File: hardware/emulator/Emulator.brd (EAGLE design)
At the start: 69.6 x 71 mm, 41 parts, among them T2 2N5401, U2 LM6132BIN, U3 OPA2277PA, U4 L7908CV, U5 L7808ABV, U7 ZVP2106ASTZ, U8 DEV-16771_REDUCED_PINS, U9 MCP4822-E/P

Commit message: Add minor changes to the hardware
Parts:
- R_RANGE: value 51R -> 49R9
- moved C5 0.51 mm to (28.4, 23.1)
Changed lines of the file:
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@@
 <attribute name="VALUE" x="53.72099375" y="32.2326" size="1.27" layer="25" ratio="10" rot="R270"/>
 </element>
-<element name="R_RANGE" library="rcl" library_urn="urn:adsk.eagle:library:334" package="0207/10" package3d_urn="urn:adsk.eagle:package:23491/2" value="51R" x="48.93733125" y="30.988" smashed="yes" rot="R270">
+<element name="R_RANGE" library="rcl" library_urn="urn:adsk.eagle:library:334" package="0207/10" package3d_urn="urn:adsk.eagle:package:23491/2" value="49R9" x="48.93733125" y="30.988" smashed="yes" rot="R270">
 <attribute name="NAME" x="48.30233125" y="43.561" size="1.016" layer="25" ratio="10" rot="R270"/>
 <attribute name="POPULARITY" value="81" x="43.85733125" y="67.564" size="1.778" layer="27" rot="R270" display="off"/>
 <attribute name="SPICEPREFIX" value="R" x="43.85733125" y="67.564" size="1.778" layer="27" rot="R270" display="off"/>
-<attribute name="VALUE" x="48.30233125" y="32.2326" size="1.27" layer="25" ratio="10" rot="R270"/>
+<attribute name="VALUE" x="48.30233125" y="33.2486" size="1.27" layer="25" ratio="10" rot="R270"/>
 </element>
 <element name="R7" library="rcl" library_urn="urn:adsk.eagle:library:334" package="0207/10" package3d_urn="urn:adsk.eagle:package:23491/2" value="100R" x="51.6466625" y="30.988" smashed="yes" rot="R270">
@@
 <attribute name="POPULARITY" value="81" x="56.7266625" y="50.8" size="1.778" layer="27" rot="R270" display="off"/>
 <attribute name="SPICEPREFIX" value="R" x="56.7266625" y="50.8" size="1.778" layer="27" rot="R270" display="off"/>
-<attribute name="VALUE" x="51.0116625" y="33.2486" size="1.27" layer="25" ratio="10" rot="R270"/>
+<attribute name="VALUE" x="51.0116625" y="33.6296" size="1.27" layer="25" ratio="10" rot="R270"/>
 </element>
 <element name="U7" library="ZVP2106A" package="TO92-SGD" value="ZVP2106ASTZ" x="60.452" y="39.624" smashed="yes" rot="R90">
@@
 </element>
 <element name="C4" library="rcl" library_urn="urn:adsk.eagle:library:334" package="C025-024X044" package3d_urn="urn:adsk.eagle:package:23630/1" value="0.1u" x="42.418" y="31.242" smashed="yes" rot="R90">
-<attribute name="NAME" x="43.688" y="34.925" size="1.016" layer="25" ratio="10" rot="R180"/>
+<attribute name="NAME" x="43.18" y="34.798" size="1.016" layer="25" ratio="10" rot="R180"/>
 <attribute name="POPULARITY" value="56" x="42.418" y="31.242" size="1.778" layer="27" rot="R90" display="off"/>
 <attribute name="SPICEPREFIX" value="C" x="42.418" y="31.242" size="1.778" layer="27" rot="R90" display="off"/>
-<attribute name="VALUE" x="43.815" y="33.02" size="1.016" layer="27" ratio="10" rot="R270"/>
-</element>
-<element name="C5" library="rcl" library_urn="urn:adsk.eagle:library:334" package="C025-024X044" package3d_urn="urn:adsk.eagle:package:23630/1" value="0.1u" x="28.448" y="23.622" smashed="yes" rot="R90">
-<attribute name="NAME" x="29.083" y="21.209" size="1.016" layer="25" ratio="10" rot="R180"/>
-<attribute name="POPULARITY" value="56" x="28.448" y="23.622" size="1.778" layer="27" rot="R90" display="off"/>
-<attribute name="SPICEPREFIX" value="C" x="28.448" y="23.622" size="1.778" layer="27" rot="R90" display="off"/>
-<attribute name="VALUE" x="27.051" y="22.352" size="1.016" layer="25" ratio="10" rot="R90"/>
+<attribute name="VALUE" x="41.021" y="27.813" size="1.016" layer="25" ratio="10"/>
+</element>
+<element name="C5" library="rcl" library_urn="urn:adsk.eagle:library:334" package="C025-024X044" package3d_urn="urn:adsk.eagle:package:23630/1" value="0.1u" x="28.448" y="23.114" smashed="yes" rot="R90">
+<attribute name="NAME" x="29.083" y="20.701" size="1.016" layer="25" ratio="10" rot="R180"/>
+<attribute name="POPULARITY" value="56" x="28.448" y="23.114" size="1.778" layer="27" rot="R90" display="off"/>
+<attribute name="SPICEPREFIX" value="C" x="28.448" y="23.114" size="1.778" layer="27" rot="R90" display="off"/>
+<attribute name="VALUE" x="27.051" y="21.844" size="1.016" layer="25" ratio="10" rot="R90"/>
 </element>
 <element name="C6" library="rcl" library_urn="urn:adsk.eagle:library:334" package="C025-024X044" package3d_urn="urn:adsk.eagle:package:23630/1" value="0.1u" x="61.214" y="19.177" smashed="yes">
-<attribute name="NAME" x="58.801" y="17.907" size="1.016" layer="25" ratio="10" rot="R90"/>
+<attribute name="NAME" x="58.801" y="18.288" size="1.016" layer="25" ratio="10" rot="R90"/>
 <attribute name="POPULARITY" value="56" x="61.214" y="19.177" size="1.778" layer="27" display="off"/>
 <attribute name="SPICEPREFIX" value="C" x="61.214" y="19.177" size="1.778" layer="27" display="off"/>
-<attribute name="VALUE" x="59.944" y="16.51" size="1.016" layer="27" ratio="10"/>
+<attribute name="VALUE" x="59.944" y="16.51" size="1.016" layer="25" ratio="10"/>
 </element>
 <element name="R6" library="rcl" library_urn="urn:adsk.eagle:library:334" package="0207/10" package3d_urn="urn:adsk.eagle:package:23491/2" value="330R" x="51.816" y="61.468" smashed="yes" rot="R180">
-<attribute name="NAME" x="52.832" y="64.008" size="1.016" layer="25" ratio="10" rot="R180"/>
+<attribute name="NAME" x="52.324" y="64.008" size="1.016" layer="25" ratio="10" rot="R180"/>
 <attribute name="POPULARITY" value="81" x="51.816" y="54.356" size="1.778" layer="27" rot="R180" display="off"/>
 <attribute name="SPICEPREFIX" value="R" x="51.816" y="54.356" size="1.778" layer="27" rot="R180" display="off"/>
@@
 </element>
 <element name="R11" library="rcl" library_urn="urn:adsk.eagle:library:334" package="0207/10" package3d_urn="urn:adsk.eagle:package:23491/2" value="330R" x="51.816" y="57.912" smashed="yes" rot="R180">
-<attribute name="NAME" x="53.34" y="56.388" size="1.016" layer="25" ratio="10" rot="R180"/>
+<attribute name="NAME" x="52.832" y="56.388" size="1.016" layer="25" ratio="10" rot="R180"/>
 <attribute name="POPULARITY" value="81" x="51.816" y="50.8" size="1.778" layer="27" rot="R180" display="off"/>
 <attribute name="SPICEPREFIX" value="R" x="51.816" y="50.8" size="1.778" layer="27" rot="R180" display="off"/>
@@
 <wire x1="44.45" y1="15.748" x2="40.132" y2="15.748" width="1.27" layer="1"/>
 <wire x1="40.132" y1="15.748" x2="39.878" y2="16.002" width="1.27" layer="1"/>
-<wire x1="28.448" y1="24.892" x2="31.496" y2="24.892" width="1.27" layer="1"/>
+<wire x1="31.496" y1="24.892" x2="28.956" y2="24.892" width="1.27" layer="1"/>
+<wire x1="28.956" y1="24.892" x2="28.448" y2="24.384" width="1.27" layer="1"/>
 <wire x1="31.496" y1="24.892" x2="31.496" y2="22.987" width="1.27" layer="1"/>
 <wire x1="39.878" y1="16.002" x2="39.878" y2="13.114" width="1.27" layer="1"/>
@@
 <wire x1="27.051" y1="32.512" x2="31.496" y2="32.512" width="1.27" layer="1"/>
 <wire x1="27.051" y1="32.512" x2="25.908" y2="31.369" width="1.27" layer="1"/>
-<wire x1="25.908" y1="31.369" x2="25.908" y2="21.844" width="1.27" layer="1"/>
-<wire x1="25.908" y1="21.844" x2="28.067" y2="19.685" width="1.27" layer="1"/>
-<wire x1="28.067" y1="19.685" x2="29.591" y2="19.685" width="1.27" layer="1"/>
-<wire x1="29.591" y1="19.685" x2="38.608" y2="10.668" width="1.27" layer="1"/>
+<wire x1="25.908" y1="31.369" x2="25.908" y2="21.336" width="1.27" layer="1"/>
+<wire x1="25.908" y1="21.336" x2="28.321" y2="18.923" width="1.27" layer="1"/>
+<wire x1="28.321" y1="18.923" x2="30.353" y2="18.923" width="1.27" layer="1"/>
+<wire x1="30.353" y1="18.923" x2="38.608" y2="10.668" width="1.27" layer="1"/>
 <wire x1="38.608" y1="10.668" x2="41.369" y2="10.668" width="1.27" layer="1"/>
 <wire x1="41.369" y1="10.668" x2="42.418" y2="11.717" width="1.27" layer="1"/>

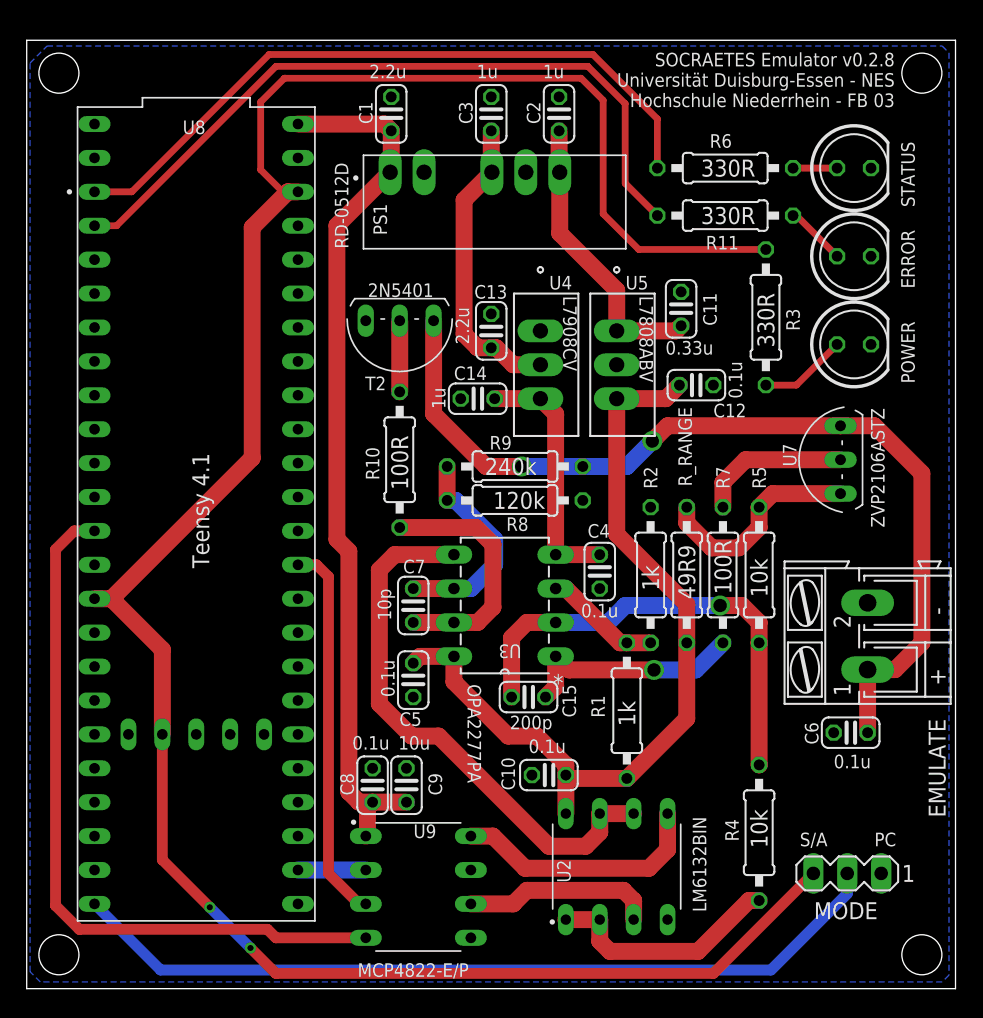
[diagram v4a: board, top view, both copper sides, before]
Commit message: Update part designators
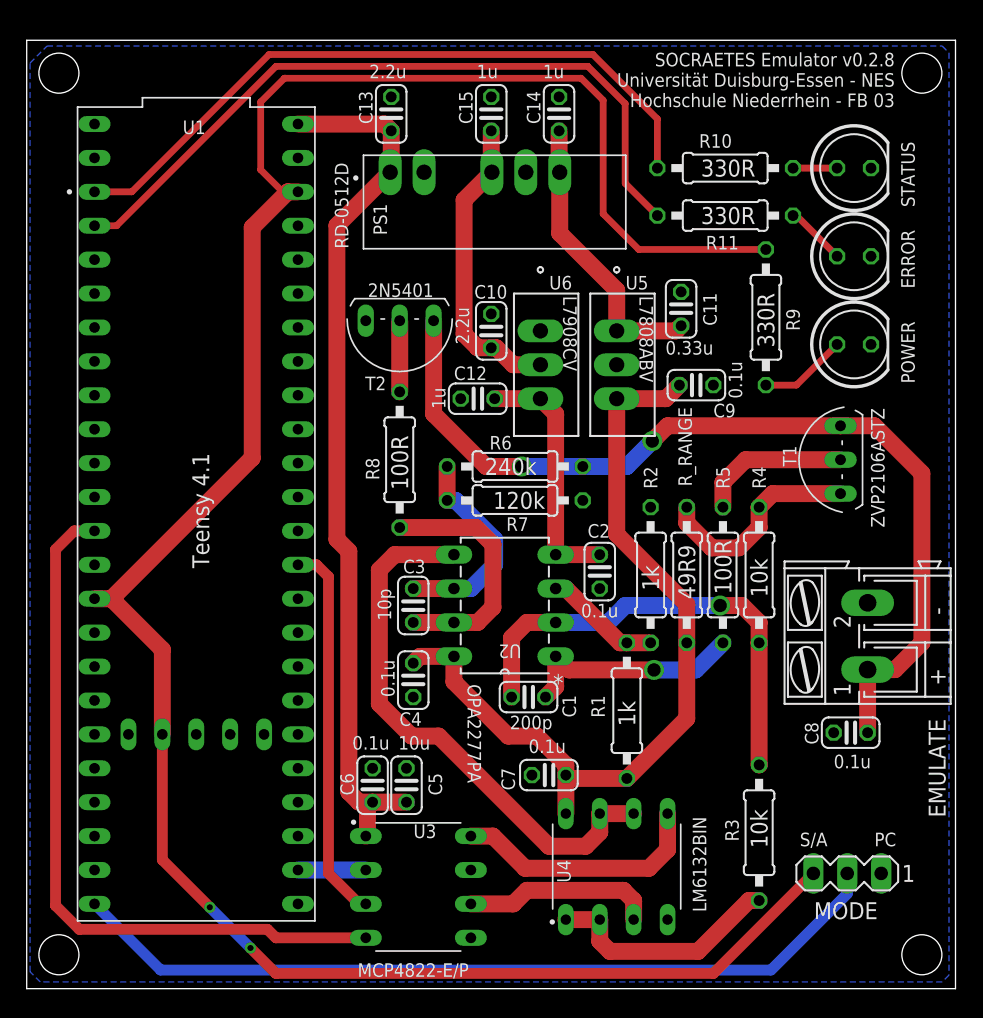
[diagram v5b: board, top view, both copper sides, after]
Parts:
- removed U9: MCP4822-E/P, MCP4822-E_P:DIP787W46P254L927H533Q8
- added U6: L7908CV, L7908CV:TO-220_STM
- C1: value 2.2u -> 200p
- C10: value 0.1u -> 2.2u
- C12: value 0.1u -> 1u
- C15: value 200p -> 1u
- C2: value 1u -> 0.1u
- C3: value 1u -> 10p
- C5: value 0.1u -> 10u
- C7: value 10p -> 0.1u
- C9: value 10u -> 0.1u
- R10: value 100R -> 330R
- R3: value 330R -> 10k
- R5: value 10k -> 100R
- R6: value 330R -> 240k
- R7: value 100R -> 120k
- R8: value 120k -> 100R
- R9: value 240k -> 330R
- U2: value LM6132BIN -> OPA2277PA; device LM6132BIN:DIP794W45P254L959H508Q8 -> OPA2277PA:P8
- U3: value OPA2277PA -> MCP4822-E/P; device OPA2277PA:P8 -> MCP4822-E_P:DIP787W46P254L927H533Q8
- U4: value L7908CV -> LM6132BIN; device L7908CV:TO-220_STM -> LM6132BIN:DIP794W45P254L959H508Q8
- moved C1 44.9 mm to (37.1, 21.8), turned to 0 degrees
- moved C15 43.8 mm to (34.3, 65.5), turned to 90 degrees
- moved U4 40.5 mm to (43.7, 9.14), turned to 90 degrees
- moved R3 38.6 mm to (54.4, 11.7), turned to 270 degrees
- moved C3 37.3 mm to (28.4, 28.7), turned to 270 degrees
- moved C9 37.0 mm to (49.7, 45.2), turned to 180 degrees
- moved C6 36.0 mm to (25.4, 15.2), turned to 90 degrees
- moved C8 36.0 mm to (61.2, 19.2), turned to 0 degrees
- moved C2 34.4 mm to (42.4, 31.2)
- moved C10 33.6 mm to (34.3, 49.3), turned to 270 degrees
- moved R10 32.7 mm to (51.8, 61.5), turned to 180 degrees
- moved R6 27.3 mm to (36.1, 39.1), turned to 0 degrees
- moved U2 26.4 mm to (31.5, 32.5), turned to 180 degrees
- moved U3 25.0 mm to (28.8, 7.62), turned to 0 degrees
- moved C14 22.2 mm to (39.4, 65.5), turned to 90 degrees
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- renumbered U7 to T1, U8 to U1
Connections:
- net +12V: now also C14.1; no longer C2.1
- net +3V3: now also R9.2; no longer R3.2
- net +5V: now also C13.1, C5.1, C6.1, U3.1; no longer C1.1, C8.1, C9.1, U9.1
- net +8V: now also C4.2, C7.2, C9.2, U4.8; no longer C10.2, C12.2, C5.2, U3.8
- net -12V: now also C10.2, C15.1, U6.2; no longer C13.2, C3.1, U4.2
- net -8V: now also C12.2, C2.2, U2.4, U6.3; no longer C14.2, C4.2, U3.4, U4.3
- net DAC_CS: now also U3.2; no longer U9.2
- net DAC_MOSI: now also U3.4; no longer U9.4
- net DAC_OC_VOLTAGE_EMULATION: now also U3.8, U4.5; no longer U2.5, U9.8
- net DAC_OC_VOLTAGE_EMULATION_BUFFERED: now also U2.5, U4.6, U4.7; no longer U2.6, U2.7, U3.5
- net DAC_SCK: now also U3.3; no longer U9.3
- net DAC_SC_CURRENT_EMULATION: now also U3.6, U4.3; no longer U2.3, U9.6
- net DAC_SC_CURRENT_EMULATION_BUFFERED: now also R3.2, U4.1, U4.2; no longer R4.2, U2.1, U2.2
- net GND: now also C13.2, C14.2, C15.2, C2.1, C5.2, C6.2, C7.1, C8.1, C9.1, R7.1, U3.5, U3.7, U4.4, U6.1; no longer C1.2, C13.1, C14.1, C2.2, C3.2, C5.1, C6.1, C8.2, C9.2, R8.1, U2.4, U4.1, U9.5, U9.7
- net HARVESTER_EMULATION: now also C8.2, R6.2; no longer C6.2, R9.2
- net N$1: now also U2.3; no longer U3.3
- net N$11: now also C3.1, R6.1, R7.2, U2.6; no longer C7.1, R8.2, R9.1, U3.6
- net N$12: now also R8.2; no longer R10.2
- net N$13: now also C3.2, R8.1, U2.7; no longer C7.2, R10.1, U3.7
- net N$2: now also R10.1; no longer R6.1
- net N$3: now also C1.1, R3.1, R4.2, U2.2; no longer C15.1, R4.1, R5.2, U3.2
- net N$5: now also R5.1; no longer R7.1
- net N$6: now also C1.2, R5.2, U2.1; no longer C15.2, R7.2, U3.1
- net N$7: now also R4.1; no longer R5.1
- net N$9: now also R9.1; no longer R3.1
- net STATUS_LED: now also R10.2; no longer R6.2

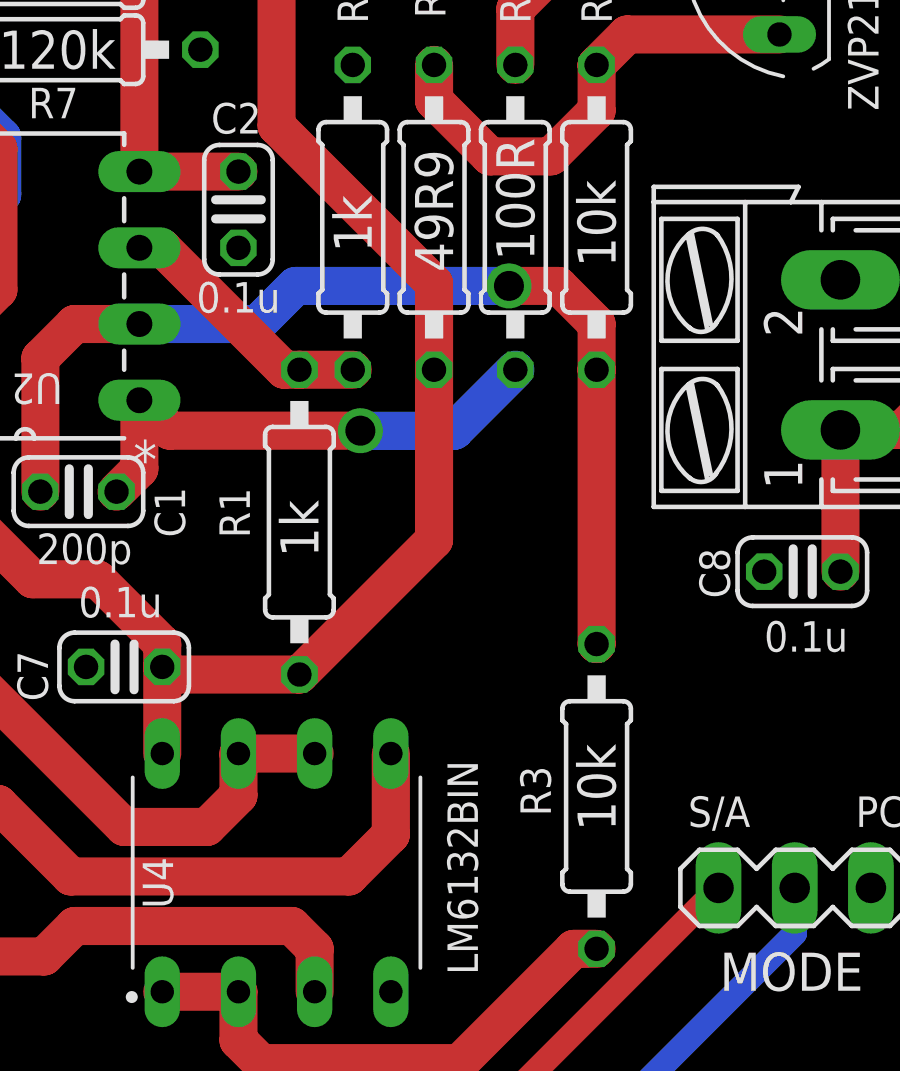
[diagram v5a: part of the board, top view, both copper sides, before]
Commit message: Update resistor values
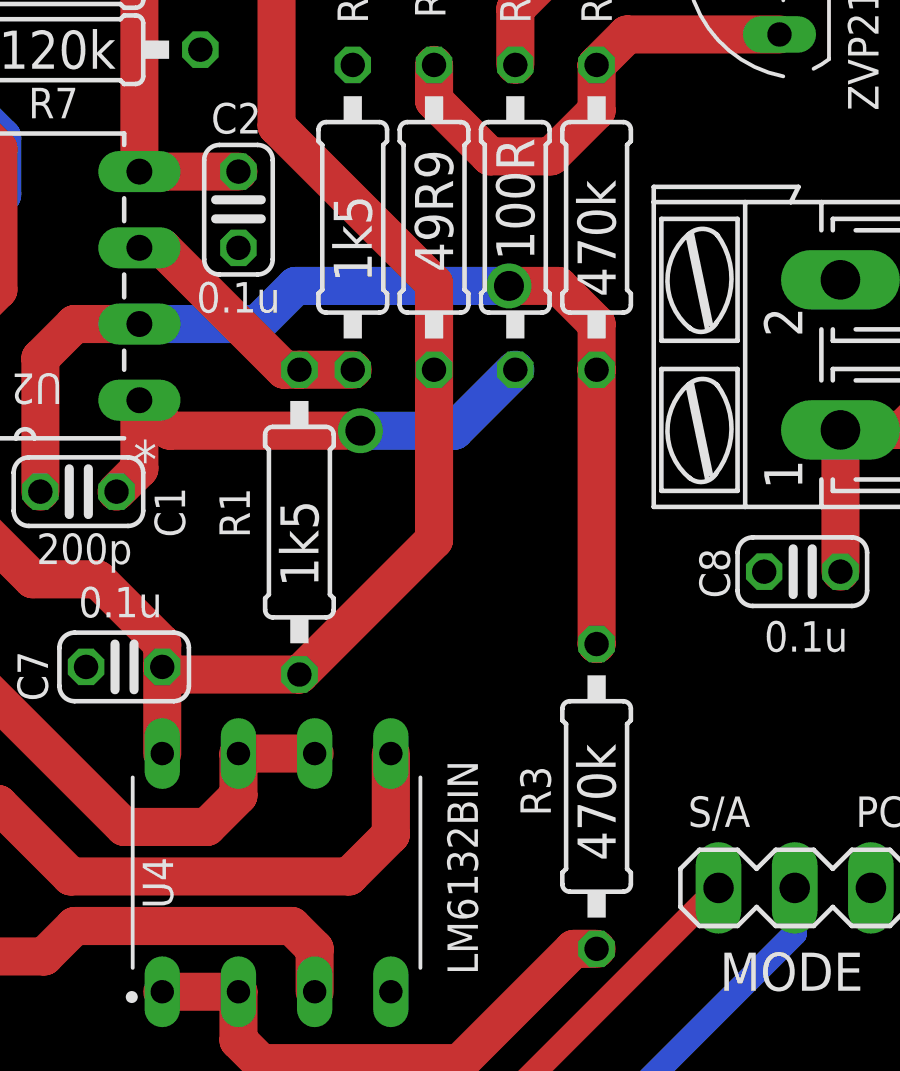
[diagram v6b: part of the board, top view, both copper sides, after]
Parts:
- R1, R2: value 1k -> 1k5
- R3, R4: value 10k -> 470k
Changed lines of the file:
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@@
 <attribute name="VENDOR" value="Texas Instruments" x="63.5" y="31.496" size="1.778" layer="27" rot="R180" display="off"/>
 </element>
-<element name="R1" library="rcl" library_urn="urn:adsk.eagle:library:334" package="0207/10" package3d_urn="urn:adsk.eagle:package:23491/2" value="1k" x="44.45" y="20.828" smashed="yes" rot="R270">
+<element name="R1" library="rcl" library_urn="urn:adsk.eagle:library:334" package="0207/10" package3d_urn="urn:adsk.eagle:package:23491/2" value="1k5" x="44.45" y="20.828" smashed="yes" rot="R270">
 <attribute name="NAME" x="41.783" y="21.971" size="1.016" layer="25" ratio="10" rot="R270"/>
 <attribute name="POPULARITY" value="81" x="63.246" y="40.64" size="1.778" layer="27" rot="R270" display="off"/>
@@
 <attribute name="VALUE" x="43.815" y="21.5646" size="1.27" layer="25" ratio="10" rot="R270"/>
 </element>
-<element name="R2" library="rcl" library_urn="urn:adsk.eagle:library:334" package="0207/10" package3d_urn="urn:adsk.eagle:package:23491/2" value="1k" x="46.228" y="30.988" smashed="yes" rot="R270">
+<element name="R2" library="rcl" library_urn="urn:adsk.eagle:library:334" package="0207/10" package3d_urn="urn:adsk.eagle:package:23491/2" value="1k5" x="46.228" y="30.988" smashed="yes" rot="R270">
 <attribute name="NAME" x="45.72" y="39.116" size="1.016" layer="25" ratio="10" rot="R270"/>
 <attribute name="POPULARITY" value="81" x="60.452" y="62.484" size="1.778" layer="27" rot="R270" display="off"/>
@@
 <attribute name="VALUE" x="45.593" y="31.7246" size="1.27" layer="25" ratio="10" rot="R270"/>
 </element>
-<element name="R3" library="rcl" library_urn="urn:adsk.eagle:library:334" package="0207/10" package3d_urn="urn:adsk.eagle:package:23491/2" value="10k" x="54.356" y="11.684" smashed="yes" rot="R270">
+<element name="R3" library="rcl" library_urn="urn:adsk.eagle:library:334" package="0207/10" package3d_urn="urn:adsk.eagle:package:23491/2" value="470k" x="54.356" y="11.684" smashed="yes" rot="R270">
 <attribute name="NAME" x="51.816" y="12.7" size="1.016" layer="25" ratio="10" rot="R270"/>
 <attribute name="POPULARITY" value="81" x="68.58" y="31.496" size="1.778" layer="27" rot="R270" display="off"/>
@@
 <attribute name="VALUE" x="53.721" y="13.4366" size="1.27" layer="25" ratio="10" rot="R270"/>
 </element>
-<element name="R4" library="rcl" library_urn="urn:adsk.eagle:library:334" package="0207/10" package3d_urn="urn:adsk.eagle:package:23491/2" value="10k" x="54.35599375" y="30.988" smashed="yes" rot="R270">
+<element name="R4" library="rcl" library_urn="urn:adsk.eagle:library:334" package="0207/10" package3d_urn="urn:adsk.eagle:package:23491/2" value="470k" x="54.35599375" y="30.988" smashed="yes" rot="R270">
 <attribute name="NAME" x="53.84799375" y="39.116" size="1.016" layer="25" ratio="10" rot="R270"/>
 <attribute name="POPULARITY" value="81" x="64.00799375" y="62.484" size="1.778" layer="27" rot="R270" display="off"/>
